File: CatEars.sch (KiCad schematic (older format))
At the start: 14 parts, among them J0 Conn_01x03_Female, J1 Conn_01x03_Female

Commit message: Added schematic and copper
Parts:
- removed J0, J1: Conn_01x03_Female, Connector_PinSocket_2.54mm:PinSocket_1x03_P2.54mm_Vertical, symbol Connector:Conn_01x03_Female
- removed JP0: SolderJumper_2_Open, Jumper:SolderJumper-2_P1.3mm_Open_TrianglePad1.0x1.5mm, symbol Jumper:SolderJumper_2_Open
- added C5, C6, C7, C8: C, Capacitor_SMD:C_0603_1608Metric_Pad1.05x0.95mm_HandSolder, symbol Device:C
- added D5, D6: LED, LED_SMD:LED_0805_2012Metric_Pad1.15x1.40mm_HandSolder, symbol Device:LED
- added D7, D8: D_Schottky, Diode_SMD:D_SOT-23_ANK, symbol Device:D_Schottky
- added H1: MountingHole_Pad, TestPoint:TestPoint_Pad_D1.5mm, symbol Mechanical:MountingHole_Pad
- added J1: Conn_01x02_Male, Connector_JST:JST_PH_B2B-PH-K_1x02_P2.00mm_Vertical, symbol Connector:Conn_01x02_Male
- added J2: USB_B_Micro, Connector_USB:USB_Micro-B_GCT_USB3076-30-A, symbol Connector:USB_B_Micro
- added J3: Conn_01x03, Connector_PinSocket_2.54mm:PinSocket_1x03_P2.54mm_Vertical, symbol Connector_Generic:Conn_01x03
- added J4, J5, J6, J7: Conn_01x01, TestPoint:TestPoint_Pad_D1.0mm, symbol Connector_Generic:Conn_01x01
- added JP1, JP2: SolderJumper_2_Open, Jumper:SolderJumper-2_P1.3mm_Open_TrianglePad1.0x1.5mm, symbol Jumper:SolderJumper_2_Open
- added R2, R3: R, Resistor_SMD:R_0805_2012Metric_Pad1.15x1.40mm_HandSolder, symbol Device:R
- added SW1: SW_Push, Button_Switch_SMD:SW_SPST_TL3342, symbol Switch:SW_Push
- added U1: ATSAMD21E18A-AU, Package_QFP:TQFP-32_7x7mm_P0.8mm, symbol 2020-01-10_20-18-23:ATSAMD21E18A-AU
- added U2: AP2112K-3.3, Package_TO_SOT_SMD:SOT-23-5, symbol Regulator_Linear:AP2112K-3.3
- R1: footprint Capacitor_SMD:C_0805_2012Metric_Pad1.15x1.40mm_HandSolder -> Resistor_SMD:R_0805_2012Metric_Pad1.15x1.40mm_HandSolder
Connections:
- net +3V3: now also C6.1, C8.1, J3.1 (Pin_1), R2.1, U1.30 (VDDIN), U1.9 (VDDANA), U2.5 (VOUT)
- net GND: now also C5.1, C6.2, C7.2, C8.2, D5.1 (K), D6.1 (K), J1.1 (Pin_1), J2.5 (GND), J3.3 (Pin_3), SW1.2, U2.2 (GND)
- net at R1.1: now also U1.13 (PA10)
- net at D4.2 (DOUT): now also JP1.1 (A)
- net at D0.4 (DIN): now also JP2.2 (B), R3.2; no longer R1.2
- new net: C7.1, D7.1 (K), D8.1 (K), U2.1 (VIN), U2.3 (EN)
- new net: R3.1, U1.11 (PA08)
- new net: SW1.1, U1.26 (*RESET)
- new net: C5.2, U1.29 (VDDCORE)
- new net: H1.1, U1.3 (PA02)
- new net: J4.1 (Pin_1), U1.31 (PA30)
- new net: J5.1 (Pin_1), U1.32 (PA31)
- new net: J7.1 (Pin_1), U1.7 (PA06)
- new net: J6.1 (Pin_1), U1.8 (PA07)
- new net: D5.2 (A), R1.2
- new net: D6.2 (A), R2.2
- new net: J3.2 (Pin_2), JP1.2 (B), JP2.1 (A)
- new net +BATT: D8.2 (A), J1.2 (Pin_2)
- new net USB_D+: J2.3 (D+), U1.24 (PA25)
- new net USB_D-: J2.2 (D-), U1.23 (PA24)
- new net VBUS: D7.2 (A), J2.1 (VBUS)
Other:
- moved on the sheet: C0, C1, C2, C3, C4, D0, D1, D2, D3, D4

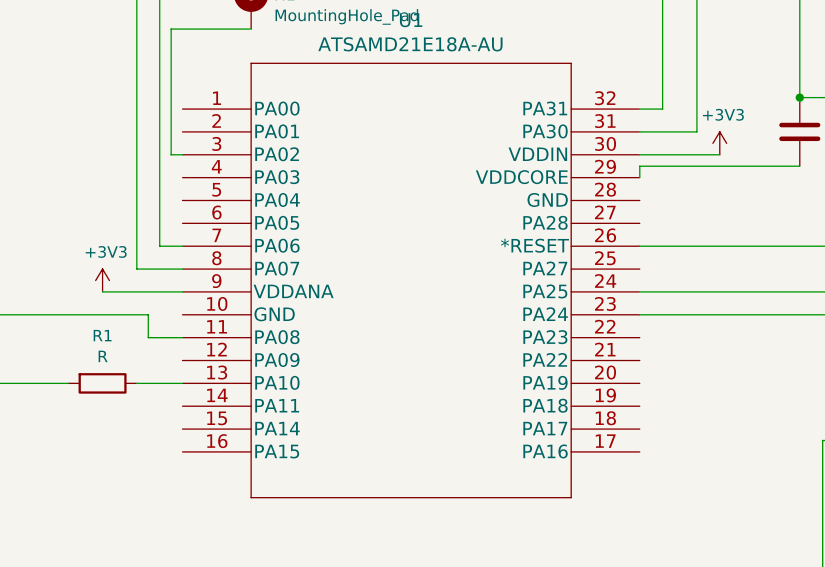
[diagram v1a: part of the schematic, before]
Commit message: v2.1 - fix unconnected GND
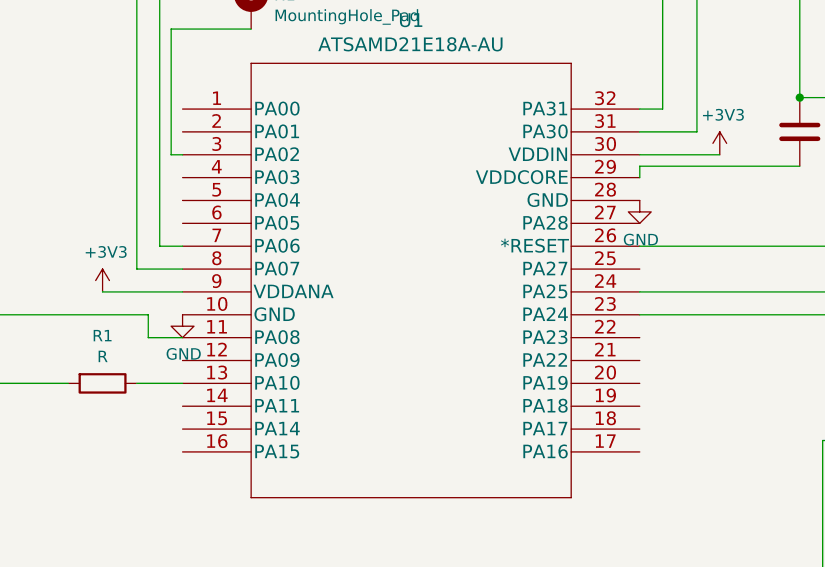
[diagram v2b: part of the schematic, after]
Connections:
- net GND: now also U1.10 (GND), U1.28 (GND)
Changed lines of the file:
@@
 Text Label 6050 1750 0    50   ~ 0
 USB_D-
+$Comp
+L power:GND #PWR?
+U 1 1 5E26A250
+P 4600 2700
+F 0 "#PWR?" H 4600 2450 50  0001 C CNN
+F 1 "GND" H 4605 2527 50  0000 C CNN
+F 2 "" H 4600 2700 50  0001 C CNN
+F 3 "" H 4600 2700 50  0001 C CNN
+	1    4600 2700
+	1    0    0    -1
+$EndComp
+$Comp
+L power:GND #PWR?
+U 1 1 5E26B38F
+P 2600 3200
+F 0 "#PWR?" H 2600 2950 50  0001 C CNN
+F 1 "GND" H 2605 3027 50  0000 C CNN
+F 2 "" H 2600 3200 50  0001 C CNN
+F 3 "" H 2600 3200 50  0001 C CNN
+	1    2600 3200
+	1    0    0    -1
+$EndComp
 $EndSCHEMATC
